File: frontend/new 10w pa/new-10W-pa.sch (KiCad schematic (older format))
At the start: 33 parts, among them CN1 BREAKOUT, K1 D3002, P1 CONN_01X02, P2 CONN_02X01, P4 CONN_01X02, P5 CONN_01X02, Q1 2N7000, Q3 RD16HHF1, T1 TRANSFO, T2 OUT_TRANSF, U1 4050, U7 LP2951-50D

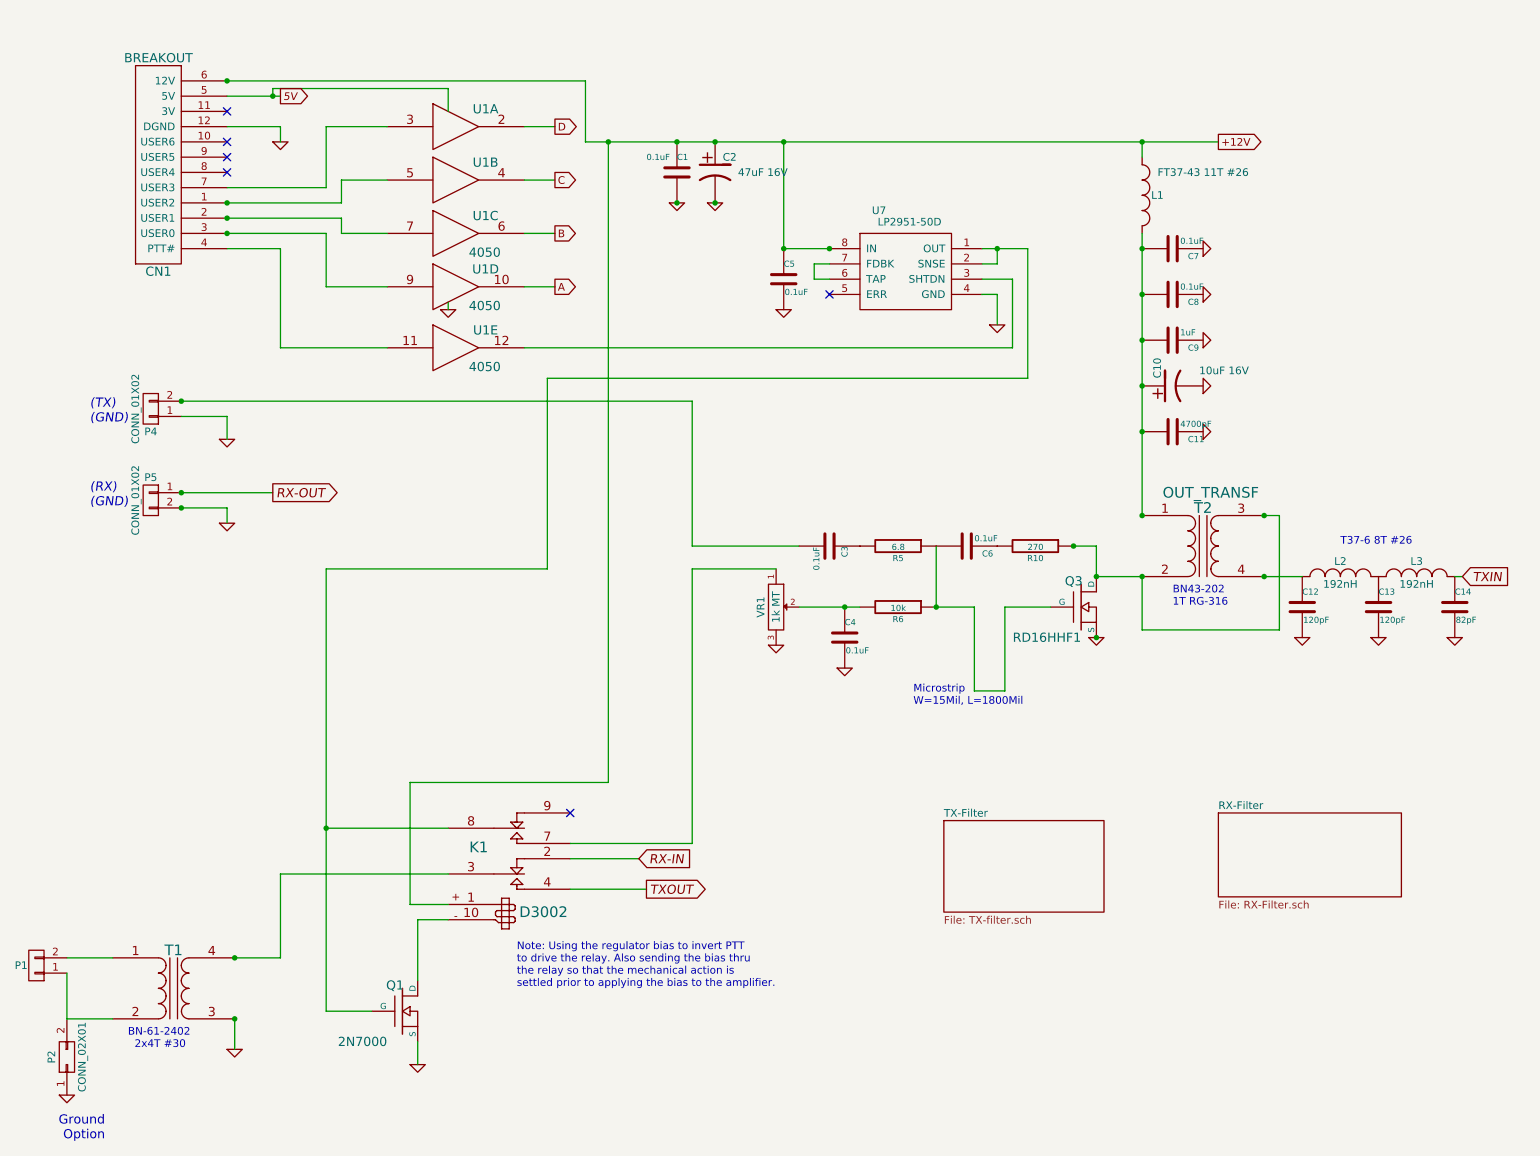
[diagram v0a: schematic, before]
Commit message: PTT change
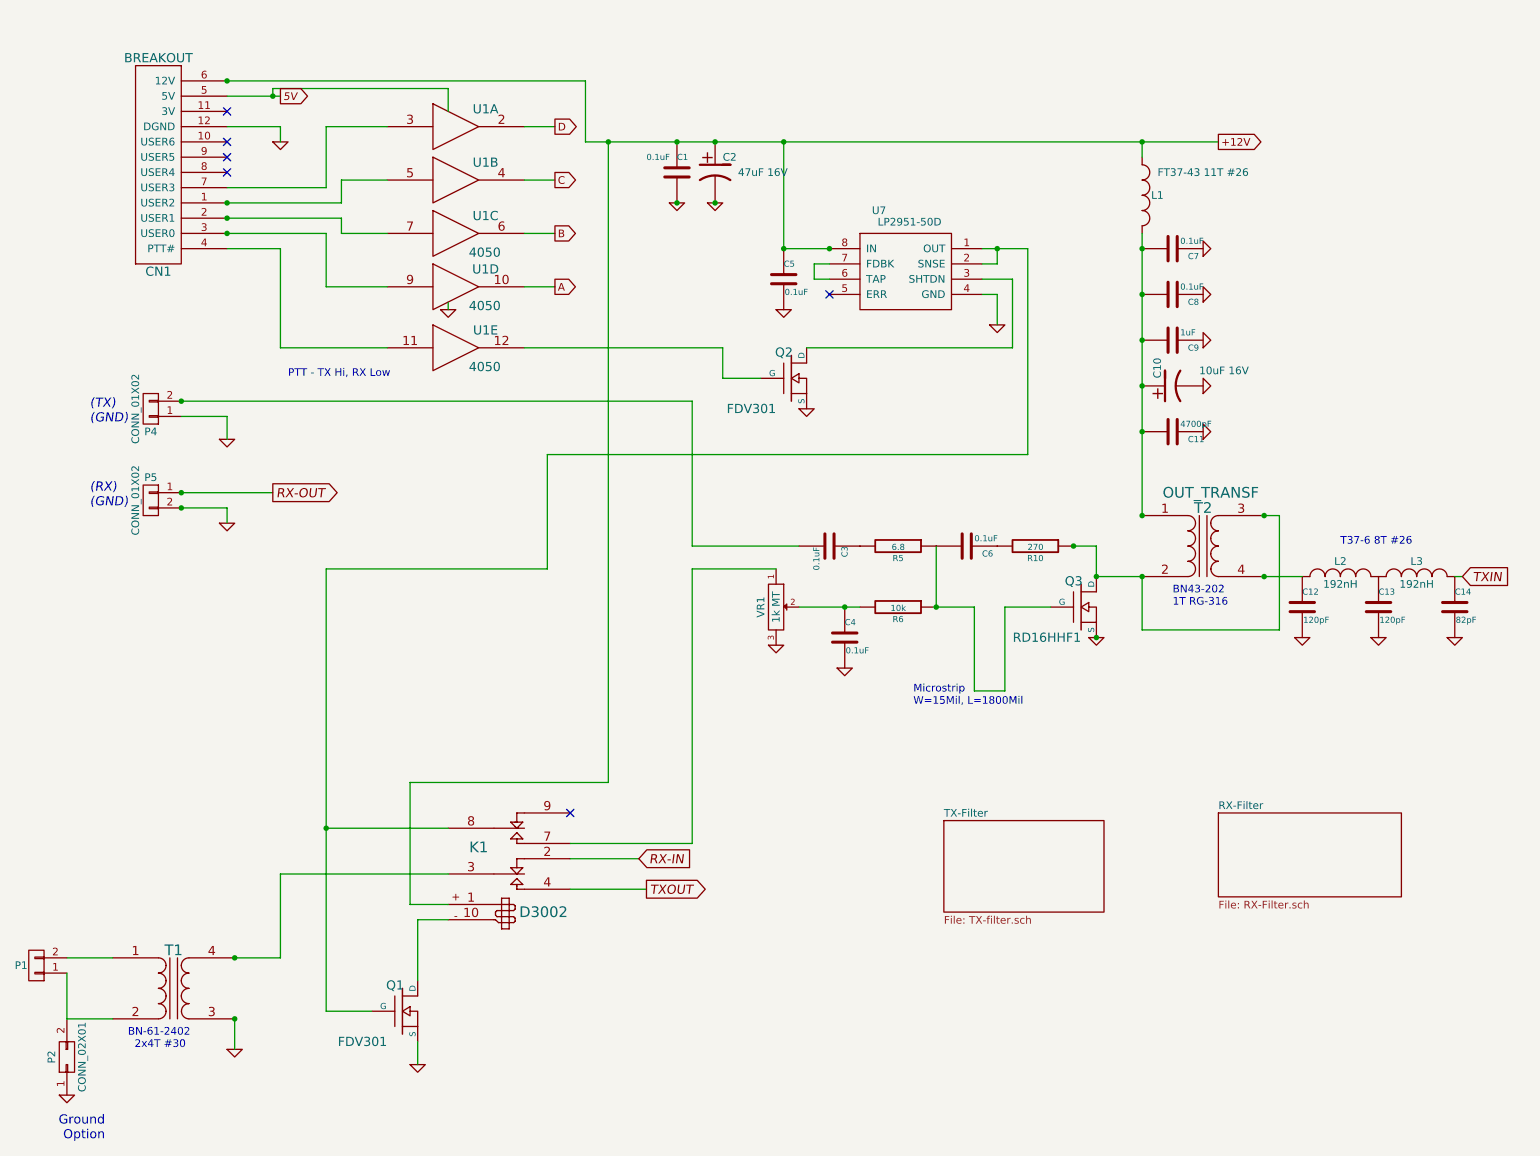
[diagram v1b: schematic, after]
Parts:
- added Q2: FDV301, SMD_Packages:SOT-23-GDS, symbol MOS_N
- Q1: value 2N7000 -> FDV301
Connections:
- net GND: now also Q2.S
- net at U7.3 (SHTDN): now also Q2.D; no longer U1.12
- new net: Q2.G, U1.12
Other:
- note added: "PTT - TX Hi, RX Low"
- note removed: "Note: Using the regulator bias to invert PTT\nto drive the relay. Also sending the bias thru\nthe relay so that the mechanical action is \nsettled prior to applying the bias to the amplifier."
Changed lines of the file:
@@
 encoding utf-8
 Sheet 1 3
-Title "Hermes-Lite Basic 5W Power Amplifier with Filters"
-Date "21 January 2015"
-Rev "1.2"
+Title "Hermes-Lite Megaband 5W Power Amplifier"
+Date "03 February 2015"
+Rev "1.21"
 Comp "SofterHardware"
-Comment1 "AC9HY"
+Comment1 "AC9HY/WA2EUJ"
 Comment2 ""
 Comment3 ""
@@
 	7000 2100 7300 2100
 Wire Wire Line
-	7300 2100 7300 2950
-Wire Wire Line
-	7300 2950 4150 2950
+	7300 2100 7300 3450
 Wire Wire Line
 	7000 2200 7100 2200
@@
 P 3200 7100
 F 0 "Q1" H 3210 7270 60  0000 R CNN
-F 1 "2N7000" H 3100 6900 60  0000 R CNN
+F 1 "FDV301" H 3100 6900 60  0000 R CNN
 F 2 "SMD_Packages:SOT-23-GDS" H 3200 7100 60  0001 C CNN
 F 3 "" H 3200 7100 60  0000 C CNN
@@
 	7200 2300 7200 2750
 Wire Wire Line
-	7200 2750 4000 2750
-Wire Wire Line
 	5800 4050 5100 4050
 Wire Wire Line
@@
 	2700 4200 4150 4200
 Wire Wire Line
-	4150 4200 4150 2950
-Wire Wire Line
 	2700 5900 3500 5900
 Connection ~ 2700 5900
@@
 Wire Wire Line
 	5100 4200 5650 4200
-Text Notes 3950 6950 0    50   ~ 0
-Note: Using the regulator bias to invert PTT\nto drive the relay. Also sending the bias thru\nthe relay so that the mechanical action is \nsettled prior to applying the bias to the amplifier.
+$Comp
+L MOS_N Q2
+U 1 1 54D0D979
+P 5750 2950
+F 0 "Q2" H 5760 3120 60  0000 R CNN
+F 1 "FDV301" H 5650 2750 60  0000 R CNN
+F 2 "SMD_Packages:SOT-23-GDS" H 5750 2950 60  0001 C CNN
+F 3 "" H 5750 2950 60  0000 C CNN
+	1    5750 2950
+	1    0    0    -1
+$EndComp
+Wire Wire Line
+	5550 2950 5300 2950
+Wire Wire Line
+	5300 2950 5300 2750
+Wire Wire Line
+	5300 2750 4000 2750
+Wire Wire Line
+	7200 2750 5850 2750
+$Comp
+L GND #PWR023
+U 1 1 54D0DD55
+P 5850 3150
+F 0 "#PWR023" H 5850 3150 30  0001 C CNN
+F 1 "GND" H 5850 3080 30  0001 C CNN
+F 2 "" H 5850 3150 50  0000 C CNN
+F 3 "" H 5850 3150 50  0000 C CNN
+	1    5850 3150
+	1    0    0    -1
+$EndComp
+Wire Wire Line
+	4150 4200 4150 3450
+Wire Wire Line
+	4150 3450 7300 3450
+Text Notes 2450 2950 0    50   ~ 0
+PTT - TX Hi, RX Low
 $EndSCHEMATC

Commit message: Added opto and change of PTT
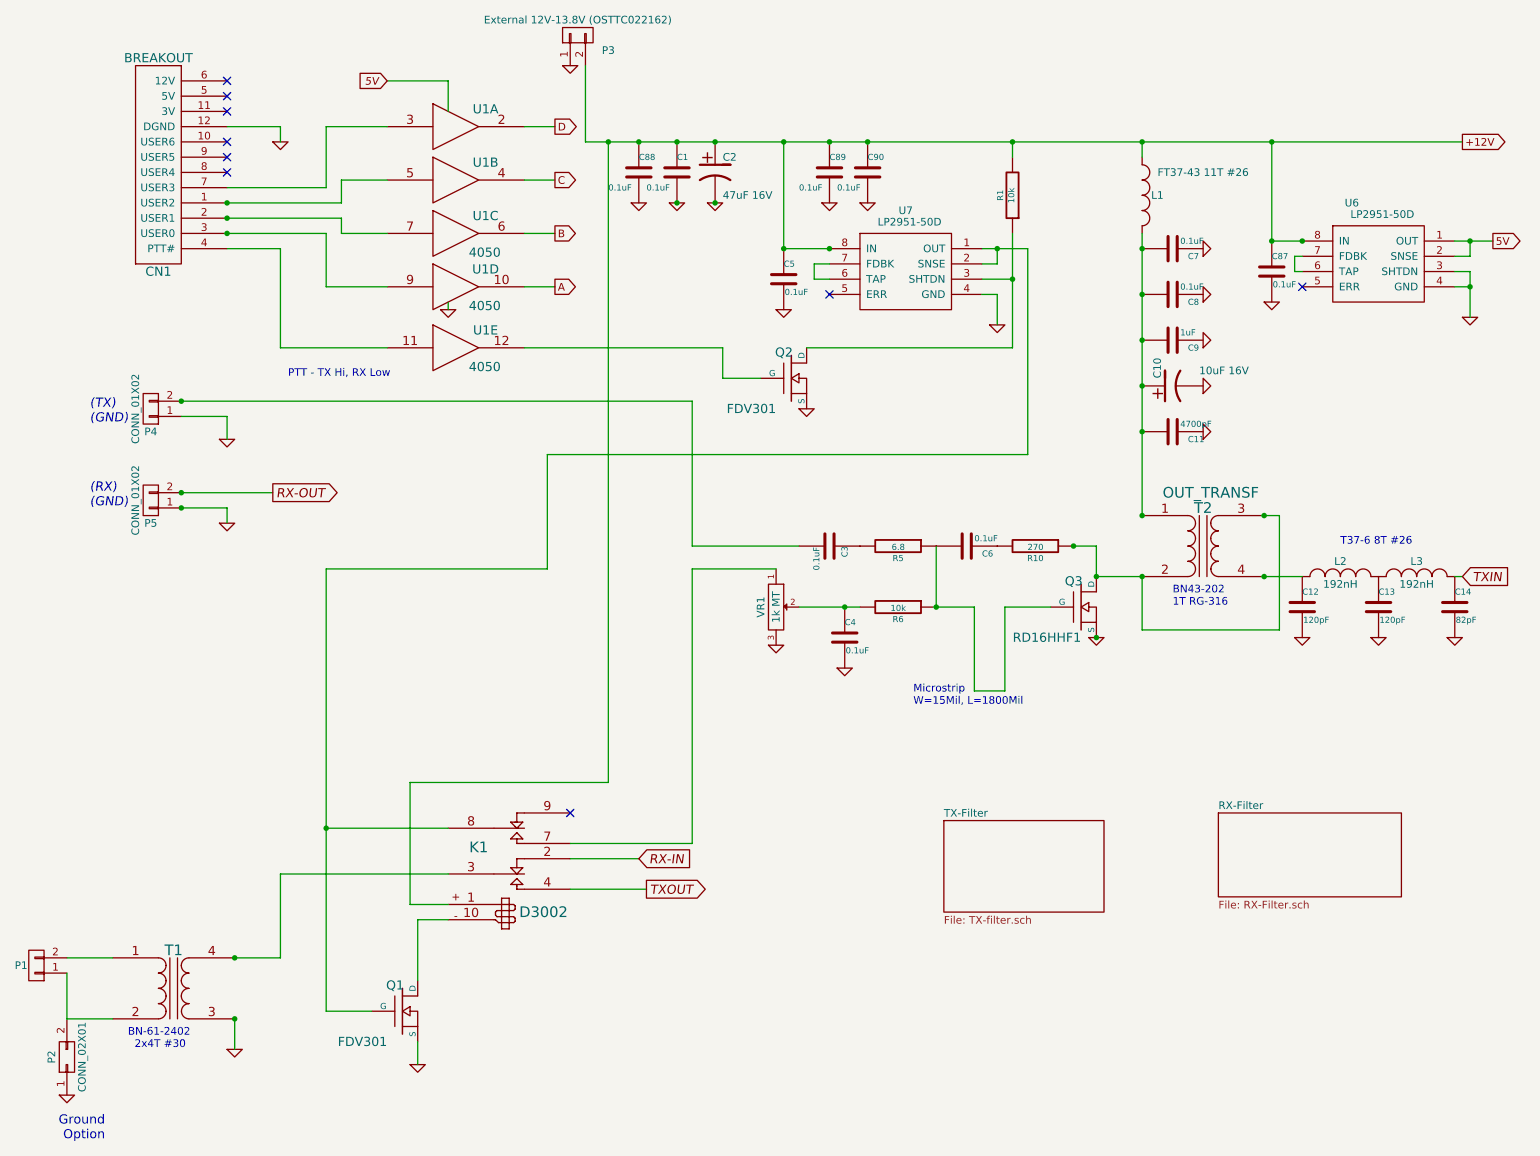
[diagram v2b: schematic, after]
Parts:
- added C87, C88, C89, C90: 0.1uF, HERMESLITE:C_0805, symbol C
- added P3: External 12V-13.8V (OSTTC022162), Connect:AK300-2, symbol CONN_01X02
- added R1: 10k, HERMESLITE:R_0805, symbol R
- added U6: LP2951-50D, Housings_SOIC:SOIC-8_3.9x4.9mm_Pitch1.27mm, symbol LP2951-50D
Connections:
- net +12V: now also C87.1, C88.1, C89.1, C90.1, P3.2 (P2), R1.2, U6.8 (IN); no longer CN1.6 (12V)
- net GND: now also P5.1 (P1), C87.2, C88.2, C89.2, C90.2, P3.1 (P1), U6.3 (SHTDN), U6.4 (GND); no longer P5.2 (P2)
- net RX-OUT: now also P5.2 (P2); no longer P5.1 (P1)
- net VCC: now also U6.1 (OUT), U6.2 (SNSE); no longer CN1.5 (5V)
- net at Q2.D, U7.3 (SHTDN): now also R1.1
- new net: U6.6 (TAP), U6.7 (FDBK)
- no-connect marks 6 -> 9
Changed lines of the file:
@@
 P 5250 1600
 F 0 "C2" H 5300 1700 50  0000 L CNN
-F 1 "47uF 16V" H 5400 1600 50  0000 L CNN
+F 1 "47uF 16V" H 5300 1450 50  0000 L CNN
 F 2 "Capacitors_Tantalum_SMD:TantalC_SizeD_EIA-7343_Reflow" H 5250 1600 60  0001 C CNN
 F 3 "" H 5250 1600 60  0000 C CNN
@@
 P 5000 1600
 F 0 "C1" H 5000 1700 40  0000 L CNN
-F 1 "0.1uF" H 4800 1700 40  0000 L CNN
+F 1 "0.1uF" H 4800 1500 40  0000 L CNN
 F 2 "HERMESLITE:C_0805" H 5038 1450 30  0001 C CNN
 F 3 "" H 5000 1600 60  0000 C CNN
@@
 Wire Wire Line
 	1000 6750 1300 6750
-Text GLabel 8550 1400 2    50   Output ~ 0
+Text GLabel 10150 1400 2    50   Output ~ 0
 +12V
 $Comp
@@
 F1 "RX-Filter.sch" 50
 $EndSheet
-Text GLabel 2400 1100 2    50   Output Italic 0
+Text GLabel 3100 1000 0    50   Input Italic 0
 5V
 Text Notes 1150 3250 0    60   Italic 0
@@
 F 3 "" H 1550 3750 60  0000 C CNN
 	1    1550 3750
-	-1   0    0    -1
+	-1   0    0    1
 $EndComp
 Wire Wire Line
@@
 Connection ~ 4550 1400
 Wire Wire Line
-	4400 1400 8550 1400
+	4400 1400 10150 1400
 $Comp
 L CP1 C10
@@
 U 1 1 54A99636
 P 6550 2450
-F 0 "U7" H 6325 3050 50  0000 C CNN
+F 0 "U7" H 6500 3050 50  0000 C CNN
 F 1 "LP2951-50D" H 6525 2975 50  0000 C CNN
 F 2 "Housings_SOIC:SOIC-8_3.9x4.9mm_Pitch1.27mm" H 6550 2450 50  0001 C CNN
@@
 $EndComp
 Wire Wire Line
-	2050 1000 4400 1000
-Wire Wire Line
-	4400 1000 4400 1400
+	4400 900  4400 1400
 Text GLabel 4200 2350 2    50   Output ~ 0
 A
@@
 Connection ~ 2050 1900
 Connection ~ 2050 1800
-Connection ~ 2050 1000
 $Comp
 L GND #PWR021
@@
 $EndComp
 Wire Wire Line
-	2050 1100 2400 1100
-Wire Wire Line
-	3500 1050 3500 1200
-Wire Wire Line
-	2350 1050 2350 1100
-Connection ~ 2350 1100
+	3500 1000 3500 1200
 Wire Wire Line
 	7000 2400 7100 2400
 Wire Wire Line
 	7100 2400 7100 2600
-Wire Wire Line
-	3500 1050 2350 1050
 $Comp
 L GND #PWR022
@@
 	7000 2300 7200 2300
 Wire Wire Line
-	7200 2300 7200 2750
+	7200 2000 7200 2750
 Wire Wire Line
 	5800 4050 5100 4050
@@
 Text Notes 2450 2950 0    50   ~ 0
 PTT - TX Hi, RX Low
+NoConn ~ 2050 1000
+Wire Wire Line
+	3100 1000 3500 1000
+$Comp
+L CONN_01X02 P3
+U 1 1 54D61932
+P 4350 700
+F 0 "P3" V 4250 500 50  0000 C CNN
+F 1 "External 12V-13.8V (OSTTC022162)" V 4450 700 50  0000 C CNN
+F 2 "Connect:AK300-2" H 4350 700 60  0001 C CNN
+F 3 "" H 4350 700 60  0000 C CNN
+	1    4350 700
+	0    -1   -1   0
+$EndComp
+$Comp
+L GND #PWR024
+U 1 1 54D61AA3
+P 4300 900
+F 0 "#PWR024" H 4300 900 30  0001 C CNN
+F 1 "GND" H 4300 830 30  0001 C CNN
+F 2 "" H 4300 900 50  0000 C CNN
+F 3 "" H 4300 900 50  0000 C CNN
+	1    4300 900
+	1    0    0    -1
+$EndComp
+$Comp
+L R R1
+U 1 1 54D62964
+P 7200 1750
+F 0 "R1" V 7280 1750 40  0000 C CNN
+F 1 "10k" V 7207 1751 40  0000 C CNN
+F 2 "HERMESLITE:R_0805" V 7130 1750 30  0001 C CNN
+F 3 "" H 7200 1750 30  0000 C CNN
+	1    7200 1750
+	-1   0    0    1
+$EndComp
+Wire Wire Line
+	7200 1400 7200 1500
+Connection ~ 7200 1400
+Connection ~ 7200 2300
+$Comp
+L LP2951-50D U6
+U 1 1 54D62F05
+P 9650 2400
+F 0 "U6" H 9425 3000 50  0000 C CNN
+F 1 "LP2951-50D" H 9625 2925 50  0000 C CNN
+F 2 "Housings_SOIC:SOIC-8_3.9x4.9mm_Pitch1.27mm" H 9650 2400 50  0001 C CNN
+F 3 "" H 9650 2400 50  0000 C CNN
+	1    9650 2400
+	1    0    0    -1
+$EndComp
+Wire Wire Line
+	9100 2050 8900 2050
+Wire Wire Line
+	8900 2050 8900 1400
+Connection ~ 8900 1400
+$Comp
+L C C87
+U 1 1 54D64DC9
+P 8900 2250
+F 0 "C87" H 8900 2350 40  0000 L CNN
+F 1 "0.1uF" H 8906 2165 40  0000 L CNN
+F 2 "HERMESLITE:C_0805" H 8938 2100 30  0001 C CNN
+F 3 "" H 8900 2250 60  0000 C CNN
+	1    8900 2250
+	1    0    0    -1
+$EndComp
+$Comp
+L GND #PWR025
+U 1 1 54D64E31
+P 8900 2450
+F 0 "#PWR025" H 8900 2450 30  0001 C CNN
+F 1 "GND" H 8900 2380 30  0001 C CNN
+F 2 "" H 8900 2450 50  0000 C CNN
+F 3 "" H 8900 2450 50  0000 C CNN
+	1    8900 2450
+	1    0    0    -1
+$EndComp
+Wire Wire Line
+	9100 2250 9050 2250
+Wire Wire Line
+	9050 2250 9050 2150
+Wire Wire Line
+	9050 2150 9100 2150
+NoConn ~ 9100 2350
+Wire Wire Line
+	10100 2250 10200 2250
+Wire Wire Line
+	10200 2250 10200 2550
+Wire Wire Line
+	10100 2350 10200 2350
+Connection ~ 10200 2350
+$Comp
+L GND #PWR026
+U 1 1 54D650E0
+P 10200 2550
+F 0 "#PWR026" H 10200 2550 30  0001 C CNN
+F 1 "GND" H 10200 2480 30  0001 C CNN
+F 2 "" H 10200 2550 50  0000 C CNN
+F 3 "" H 10200 2550 50  0000 C CNN
+	1    10200 2550
+	1    0    0    -1
+$EndComp
+Wire Wire Line
+	10100 2150 10200 2150
+Wire Wire Line
+	10200 2150 10200 2050
+Wire Wire Line
+	10100 2050 10350 2050
+Connection ~ 10200 2050
+Text GLabel 10350 2050 2    50   Output ~ 0
+5V
+NoConn ~ 2050 1100
+Connection ~ 8900 2050
+Connection ~ 9100 2050
+$Comp
+L C C88
+U 1 1 54D8CF54
+P 4750 1600
+F 0 "C88" H 4750 1700 40  0000 L CNN
+F 1 "0.1uF" H 4550 1500 40  0000 L CNN
+F 2 "HERMESLITE:C_0805" H 4788 1450 30  0001 C CNN
+F 3 "" H 4750 1600 60  0000 C CNN
+	1    4750 1600
+	1    0    0    -1
+$EndComp
+$Comp
+L C C89
+U 1 1 54D8CF9D
+P 6000 1600
+F 0 "C89" H 6000 1700 40  0000 L CNN
+F 1 "0.1uF" H 5800 1500 40  0000 L CNN
+F 2 "HERMESLITE:C_0805" H 6038 1450 30  0001 C CNN
+F 3 "" H 6000 1600 60  0000 C CNN
+	1    6000 1600
+	1    0    0    -1
+$EndComp
+$Comp
+L C C90
+U 1 1 54D8D011
+P 6250 1600
+F 0 "C90" H 6250 1700 40  0000 L CNN
+F 1 "0.1uF" H 6050 1500 40  0000 L CNN
+F 2 "HERMESLITE:C_0805" H 6288 1450 30  0001 C CNN
+F 3 "" H 6250 1600 60  0000 C CNN
+	1    6250 1600
+	1    0    0    -1
+$EndComp
+$Comp
+L GND #PWR027
+U 1 1 54D8D0A1
+P 4750 1800
+F 0 "#PWR027" H 4750 1800 30  0001 C CNN
+F 1 "GND" H 4750 1730 30  0001 C CNN
+F 2 "" H 4750 1800 60  0000 C CNN
+F 3 "" H 4750 1800 60  0000 C CNN
+	1    4750 1800
+	1    0    0    -1
+$EndComp
+$Comp
+L GND #PWR028
+U 1 1 54D8D0D9
+P 6000 1800
+F 0 "#PWR028" H 6000 1800 30  0001 C CNN
+F 1 "GND" H 6000 1730 30  0001 C CNN
+F 2 "" H 6000 1800 60  0000 C CNN
+F 3 "" H 6000 1800 60  0000 C CNN
+	1    6000 1800
+	1    0    0    -1
+$EndComp
+$Comp
+L GND #PWR029
+U 1 1 54D8D111
+P 6250 1800
+F 0 "#PWR029" H 6250 1800 30  0001 C CNN
+F 1 "GND" H 6250 1730 30  0001 C CNN
+F 2 "" H 6250 1800 60  0000 C CNN
+F 3 "" H 6250 1800 60  0000 C CNN
+	1    6250 1800
+	1    0    0    -1
+$EndComp
+Connection ~ 4750 1400
+Connection ~ 6000 1400
+Connection ~ 6250 1400
 $EndSCHEMATC
